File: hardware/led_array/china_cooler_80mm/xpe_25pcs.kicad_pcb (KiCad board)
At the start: 2 copper layers, 25 parts

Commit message: initial 80mm pcb draft ready
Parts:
- added J1: Conn_01x10, led:header_10_smd, F.Cu at (26.7, 10.2)
- D1, D10, D11, D12, D13, D14, D15, D16, D17, D18, D19, D2, D20, D21, D22, D23, D24, D25, D3, D4, D5, D6, D7, D8, D9: footprint LEDs:LED-XP-G_CREE -> led:LED_Cree-XP-E
- moved D25 3.13 mm to (39.4, 56.4)
- moved D21 3.05 mm to (39.5, 31.5)
- moved D22 3.05 mm to (39.5, 37.8)
- moved D23 3.02 mm to (39.5, 44.2)
- moved D24 3.00 mm to (39.5, 50.2)
- moved D16 2.29 mm to (35.0, 31.5)
- moved D17 2.29 mm to (35.0, 37.8)
- moved D18 2.29 mm to (35.0, 44.1)
- moved D19 2.29 mm to (35.0, 50.1)
- moved D20 2.29 mm to (34.9, 56.4)
- moved D11 1.52 mm to (30.5, 31.5)
- moved D12 1.52 mm to (30.5, 37.8)
- moved D13 1.52 mm to (30.5, 44.1)
- moved D14 1.52 mm to (30.5, 50.1)
- moved D15 1.52 mm to (30.5, 56.4)
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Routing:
- net GND: track 0.00 -> 105.4 mm
- net Net-(D1-Pad2): track 0.00 -> 30.0 mm
- net Net-(D11-Pad2): track 0.00 -> 27.3 mm
- net Net-(D21-Pad2): track 0.00 -> 25.8 mm
- net Net-(D6-Pad2): track 0.00 -> 23.4 mm
- net Net-(D16-Pad2): track 0.00 -> 20.7 mm
- net Net-(D22-Pad1): track 0.00 -> 3.66 mm
- net Net-(D7-Pad1): track 0.00 -> 3.60 mm
- net Net-(D2-Pad1): track 0.00 -> 3.60 mm
- net Net-(D17-Pad1): track 0.00 -> 3.60 mm
- net Net-(D12-Pad1): track 0.00 -> 3.60 mm
- net Net-(D24-Pad1): track 0.00 -> 3.48 mm
- net Net-(D19-Pad1): track 0.00 -> 3.47 mm
- net Net-(D6-Pad1): track 0.00 -> 3.45 mm
- net Net-(D4-Pad1): track 0.00 -> 3.45 mm
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
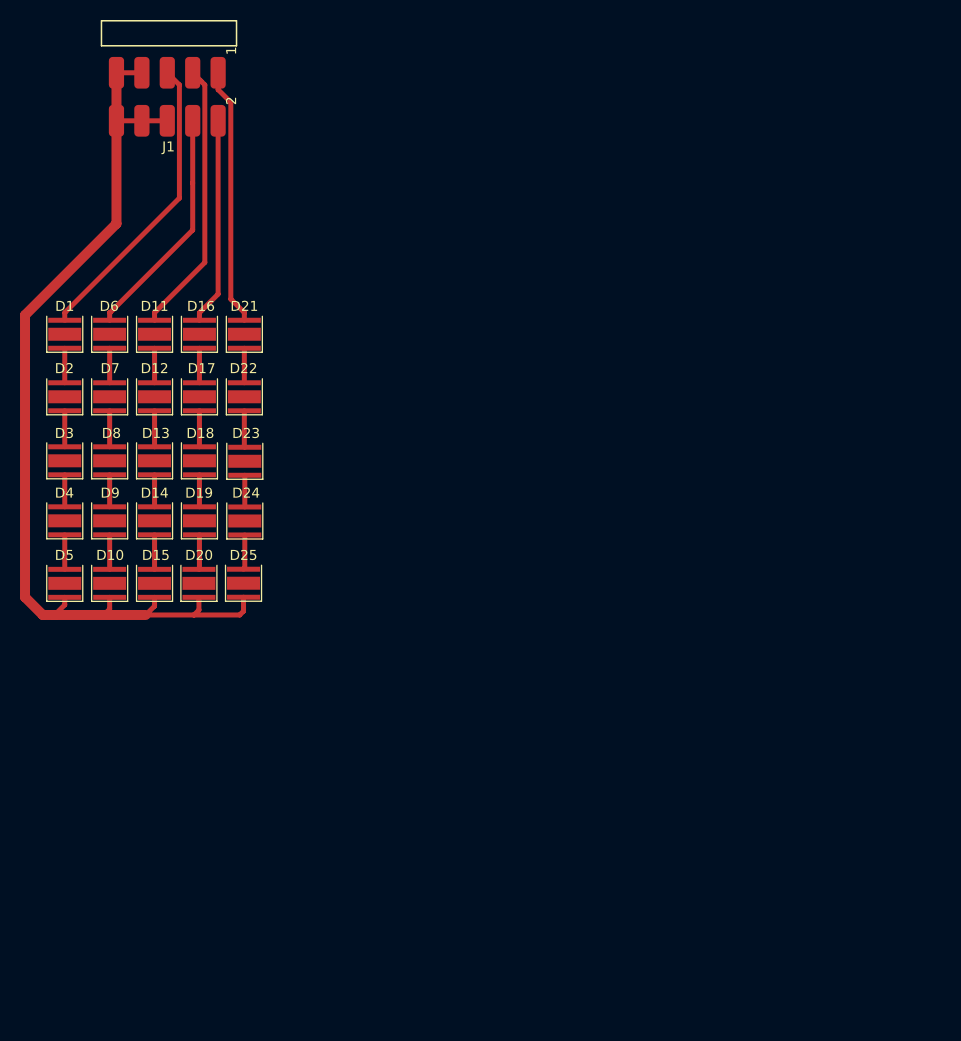
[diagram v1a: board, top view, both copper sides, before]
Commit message: 25 led array improved
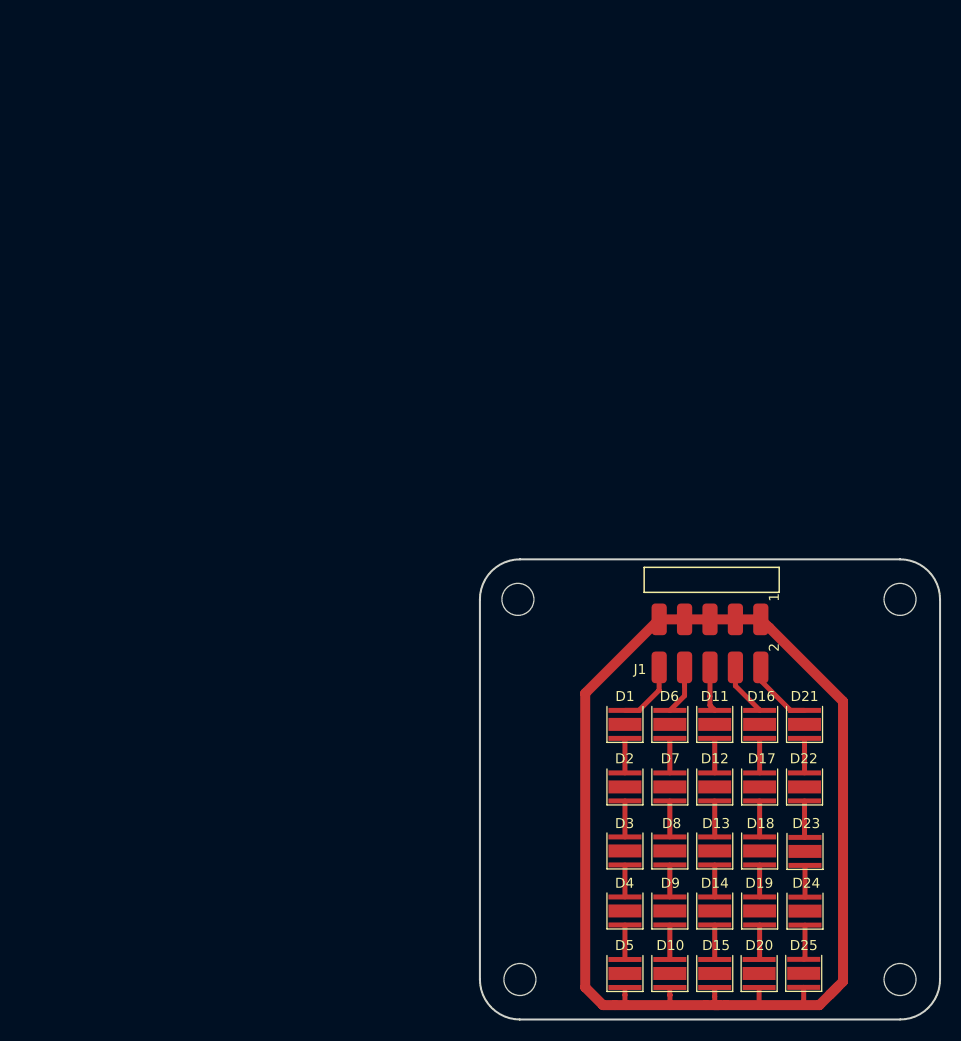
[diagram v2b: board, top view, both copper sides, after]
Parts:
- added REF**: MountingHole_3.2mm_M3_ISO7380, led:MountingHole_3.2mm_M3_ISO7380, F.Cu at (66.8, 58.0)
- added REF**: MountingHole_3.2mm_M3_ISO7380, led:MountingHole_3.2mm_M3_ISO7380, F.Cu at (105.0, 58.0)
- added REF**: MountingHole_3.2mm_M3_ISO7380, led:MountingHole_3.2mm_M3_ISO7380, F.Cu at (67.0, 96.0)
- added REF**: MountingHole_3.2mm_M3_ISO7380, led:MountingHole_3.2mm_M3_ISO7380, F.Cu at (105.0, 96.0)
- moved J1 77.0 mm to (80.9, 64.8)
- moved D25 68.2 mm to (95.4, 95.4)
- moved D10 68.2 mm to (82.0, 95.4)
- moved D13 68.2 mm to (86.5, 83.2)
- moved D14 68.2 mm to (86.5, 89.2)
- moved D15 68.2 mm to (86.5, 95.4)
- moved D18 68.2 mm to (91.0, 83.2)
- moved D19 68.2 mm to (91.0, 89.2)
- moved D20 68.2 mm to (90.9, 95.4)
- moved D24 68.2 mm to (95.5, 89.2)
- moved D3 68.2 mm to (77.5, 83.2)
- moved D4 68.2 mm to (77.5, 89.2)
- moved D5 68.2 mm to (77.5, 95.4)
- moved D8 68.2 mm to (82.0, 83.2)
- moved D9 68.2 mm to (82.0, 89.2)
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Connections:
- J1 pad 1: Net-(D21-Pad2) -> GND
- J1 pad 10: GND -> Net-(D1-Pad2)
- J1 pad 2: Net-(D16-Pad2) -> Net-(D21-Pad2)
- J1 pad 3: Net-(D11-Pad2) -> GND
- J1 pad 4: Net-(D6-Pad2) -> Net-(D16-Pad2)
- J1 pad 5: Net-(D1-Pad2) -> GND
- J1 pad 6: GND -> Net-(D11-Pad2)
- J1 pad 8: GND -> Net-(D6-Pad2)
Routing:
- net GND: track 105.4 -> 151.7 mm
- net Net-(D1-Pad2): track 30.0 -> 6.54 mm
- net Net-(D11-Pad2): track 27.3 -> 4.50 mm
- net Net-(D21-Pad2): track 25.8 -> 6.93 mm
- net Net-(D6-Pad2): track 23.4 -> 4.92 mm
- net Net-(D16-Pad2): track 20.7 -> 5.30 mm
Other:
- board outline added: 46 x 46 mm
